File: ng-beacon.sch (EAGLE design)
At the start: 7 parts

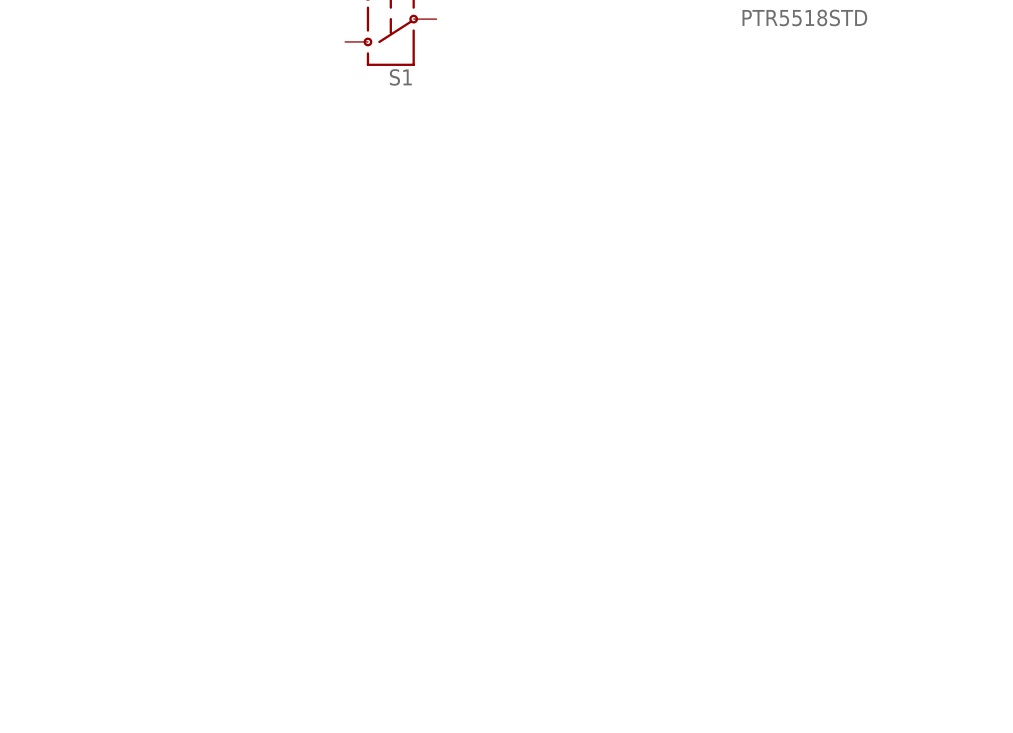
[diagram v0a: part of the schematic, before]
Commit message: feat(pcb): initial effort adding an IMU
MPU-9250: includes accelerometer, gyroscope, compass
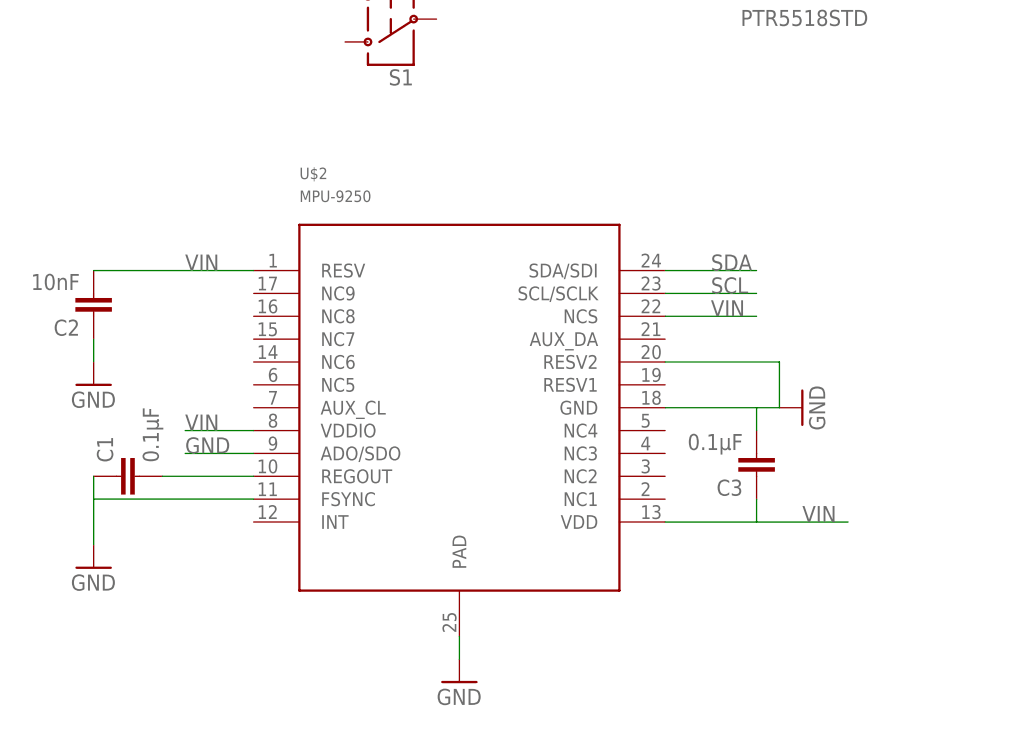
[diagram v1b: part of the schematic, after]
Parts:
- added C1, C3: 0.1µF, SparkFun-Capacitors:CAP0603-CAP
- added C2: 10nF, SparkFun-Capacitors:CAP0603-CAP
- added U$2: MPU-9250, invensense:MPU-9250
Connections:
- new net N$4: C1.2, U$2.REGOUT
- net GND: now also C1.1, C2.1, C3.2, U$2.ADO/SDO, U$2.FSYNC, U$2.GND, U$2.PAD, U$2.RESV2
- net SCL: now also U$2.SCL/SCLK
- net SDA: now also U$2.SDA/SDI
- net VIN: now also C2.2, C3.1, U$2.NCS, U$2.RESV, U$2.VDD, U$2.VDDIO
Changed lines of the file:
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@@
 <layer number="56" name="wert" color="7" fill="1" visible="no" active="no"/>
 <layer number="57" name="tCAD" color="7" fill="1" visible="no" active="no"/>
+<layer number="58" name="bCAD" color="7" fill="1" visible="no" active="no"/>
 <layer number="59" name="tCarbon" color="7" fill="1" visible="no" active="no"/>
 <layer number="60" name="bCarbon" color="7" fill="1" visible="no" active="no"/>
@@
 <part name="R1" library="SparkFun-Resistors" deviceset="10KOHM-1/10W-1%(0603)" device="0603" value="10K"/>
 <part name="R2" library="SparkFun-Resistors" deviceset="10KOHM-1/10W-1%(0603)" device="0603" value="10K"/>
+<part name="U$2" library="invensense" deviceset="MPU-9250" device=""/>
+<part name="GND5" library="SparkFun-Aesthetics" deviceset="GND" device=""/>
+<part name="GND6" library="SparkFun-Aesthetics" deviceset="GND" device=""/>
+<part name="C1" library="SparkFun-Capacitors" deviceset="CAP" device="0603-CAP" value="0.1µF"/>
+<part name="C2" library="SparkFun-Capacitors" deviceset="CAP" device="0603-CAP" value="10nF"/>
+<part name="GND9" library="SparkFun-Aesthetics" deviceset="GND" device=""/>
+<part name="C3" library="SparkFun-Capacitors" deviceset="CAP" device="0603-CAP" value="0.1µF"/>
+<part name="GND7" library="SparkFun-Aesthetics" deviceset="GND" device=""/>
 </parts>
 <sheets>
@@
 <instance part="R1" gate="G$1" x="45.72" y="93.98"/>
 <instance part="R2" gate="G$1" x="45.72" y="88.9"/>
+<instance part="U$2" gate="G$1" x="-12.7" y="2.54"/>
+<instance part="GND5" gate="1" x="25.4" y="2.54" rot="R90"/>
+<instance part="GND6" gate="1" x="-53.34" y="-15.24"/>
+<instance part="C1" gate="G$1" x="-48.26" y="-5.08" rot="R90"/>
+<instance part="C2" gate="G$1" x="-53.34" y="15.24" rot="R180"/>
+<instance part="GND9" gate="1" x="-53.34" y="5.08"/>
+<instance part="C3" gate="G$1" x="20.32" y="-2.54" rot="R180"/>
+<instance part="GND7" gate="1" x="-12.7" y="-27.94"/>
 </instances>
 <busses>
@@
 <pinref part="GND4" gate="1" pin="GND"/>
 </segment>
+<segment>
+<pinref part="GND5" gate="1" pin="GND"/>
+<pinref part="U$2" gate="G$1" pin="GND"/>
+<wire x1="22.86" y1="2.54" x2="20.32" y2="2.54" width="0.1524" layer="91"/>
+<pinref part="U$2" gate="G$1" pin="RESV2"/>
+<wire x1="20.32" y1="2.54" x2="10.16" y2="2.54" width="0.1524" layer="91"/>
+<wire x1="10.16" y1="7.62" x2="22.86" y2="7.62" width="0.1524" layer="91"/>
+<wire x1="22.86" y1="7.62" x2="22.86" y2="2.54" width="0.1524" layer="91"/>
+<pinref part="C3" gate="G$1" pin="2"/>
+<wire x1="20.32" y1="0" x2="20.32" y2="2.54" width="0.1524" layer="91"/>
+</segment>
+<segment>
+<pinref part="U$2" gate="G$1" pin="FSYNC"/>
+<pinref part="GND6" gate="1" pin="GND"/>
+<wire x1="-35.56" y1="-7.62" x2="-53.34" y2="-7.62" width="0.1524" layer="91"/>
+<pinref part="C1" gate="G$1" pin="1"/>
+<wire x1="-53.34" y1="-10.16" x2="-53.34" y2="-12.7" width="0.1524" layer="91"/>
+<wire x1="-53.34" y1="-5.08" x2="-53.34" y2="-7.62" width="0.1524" layer="91"/>
+<wire x1="-53.34" y1="-10.16" x2="-53.34" y2="-7.62" width="0.1524" layer="91"/>
+</segment>
+<segment>
+<pinref part="GND9" gate="1" pin="GND"/>
+<pinref part="C2" gate="G$1" pin="1"/>
+<wire x1="-53.34" y1="10.16" x2="-53.34" y2="7.62" width="0.1524" layer="91"/>
+</segment>
+<segment>
+<pinref part="U$2" gate="G$1" pin="ADO/SDO"/>
+<wire x1="-35.56" y1="-2.54" x2="-40.64" y2="-2.54" width="0.1524" layer="91"/>
+<wire x1="-40.64" y1="-2.54" x2="-43.18" y2="-2.54" width="0.1524" layer="91"/>
+<label x="-43.18" y="-2.54" size="1.778" layer="95"/>
+</segment>
+<segment>
+<pinref part="U$2" gate="G$1" pin="PAD"/>
+<pinref part="GND7" gate="1" pin="GND"/>
+<wire x1="-12.7" y1="-22.86" x2="-12.7" y2="-25.4" width="0.1524" layer="91"/>
+</segment>
 </net>
 <net name="N$1" class="0">
@@
 <label x="55.88" y="88.9" size="1.778" layer="95" xref="yes"/>
 </segment>
+<segment>
+<pinref part="U$2" gate="G$1" pin="VDD"/>
+<wire x1="10.16" y1="-10.16" x2="20.32" y2="-10.16" width="0.1524" layer="91"/>
+<label x="25.4" y="-10.16" size="1.778" layer="95"/>
+<pinref part="C3" gate="G$1" pin="1"/>
+<wire x1="20.32" y1="-10.16" x2="30.48" y2="-10.16" width="0.1524" layer="91"/>
+<wire x1="20.32" y1="-7.62" x2="20.32" y2="-10.16" width="0.1524" layer="91"/>
+</segment>
+<segment>
+<pinref part="U$2" gate="G$1" pin="VDDIO"/>
+<wire x1="-35.56" y1="0" x2="-43.18" y2="0" width="0.1524" layer="91"/>
+<label x="-43.18" y="0" size="1.778" layer="95"/>
+</segment>
+<segment>
+<pinref part="U$2" gate="G$1" pin="RESV"/>
+<wire x1="-35.56" y1="17.78" x2="-53.34" y2="17.78" width="0.1524" layer="91"/>
+<label x="-43.18" y="17.78" size="1.778" layer="95"/>
+<pinref part="C2" gate="G$1" pin="2"/>
+</segment>
+<segment>
+<pinref part="U$2" gate="G$1" pin="NCS"/>
+<wire x1="10.16" y1="12.7" x2="20.32" y2="12.7" width="0.1524" layer="91"/>
+<label x="15.24" y="12.7" size="1.778" layer="95"/>
+</segment>
 </net>
 <net name="SWCLK" class="0">
@@
 <label x="35.56" y="93.98" size="1.778" layer="95" rot="R180" xref="yes"/>
 </segment>
+<segment>
+<pinref part="U$2" gate="G$1" pin="SDA/SDI"/>
+<wire x1="10.16" y1="17.78" x2="20.32" y2="17.78" width="0.1524" layer="91"/>
+<label x="15.24" y="17.78" size="1.778" layer="95"/>
+</segment>
 </net>
 <net name="SCL" class="0">
@@
 <label x="35.56" y="88.9" size="1.778" layer="95" rot="R180" xref="yes"/>
 </segment>
-</net>
+<segment>
+<pinref part="U$2" gate="G$1" pin="SCL/SCLK"/>
+<wire x1="10.16" y1="15.24" x2="20.32" y2="15.24" width="0.1524" layer="91"/>
+<label x="15.24" y="15.24" size="1.778" layer="95"/>
+</segment>
+</net>
+<net name="N$4" class="0">
+<segment>
+<pinref part="U$2" gate="G$1" pin="REGOUT"/>
+<pinref part="C1" gate="G$1" pin="2"/>
+<wire x1="-45.72" y1="-5.08" x2="-35.56" y2="-5.08" width="0.1524" layer="91"/>
+</segment>
+</net>
